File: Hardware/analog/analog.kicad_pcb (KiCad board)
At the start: 4 copper layers, 128 x 182 mm, 131 parts, among them J201 Würth 74651194R, J202 Würth 74651194R, J301 Conn_02x10_Odd_Even, J501 Conn_01x01, J502 Conn_01x01, M501 Fan_4pin, Q201 IXTH80N075L2, Q202 IXTH80N075L2, Q501 MMBT3904, U201 ADA4522-2, U202 LM431SC, U203 LMT86LMT, U204 ADA4522-2, U205 LM431SC, U206 LMT86LMT, U301 ADUM131D, U302 ADUM131D, U303 ADUM1250, U304 74LVC1G19, U305 AT24CS32-SSHM, U401 ICL7660, U402 MCP1804x-C002xMB, U403 MCP1703AT-5002E/DB, U404 XC6203E33, U405 LP5907MFX-3.3, U501 EMC2101-R, U601 MCP3562, U602 MAX6166, U603 DAC8562, U701 Si5351A-B-GT, Y701 25MHz

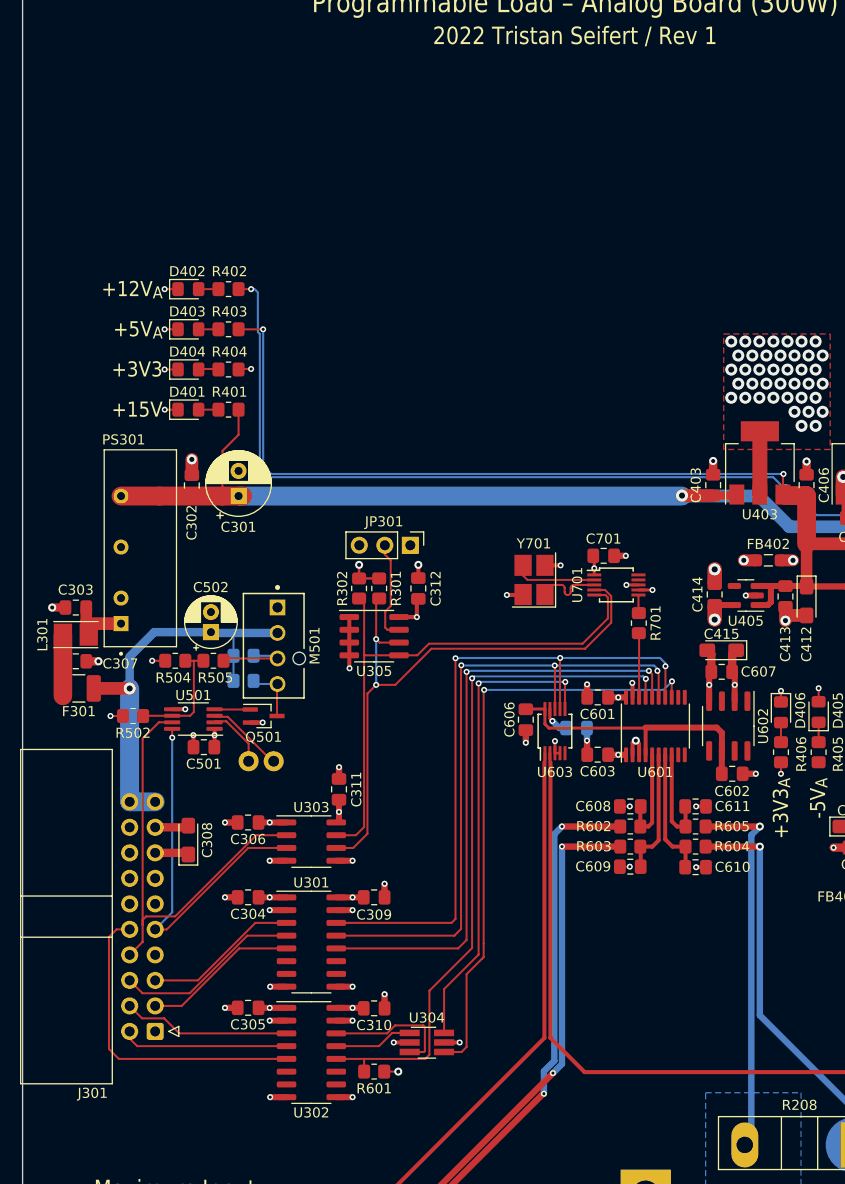
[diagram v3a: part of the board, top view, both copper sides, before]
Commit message: Moved analog board connector
- It now lines up properly with the one on the controller after it's
  been moved; there's still a bunch of un-done (power supply) stuff that
  needs to be re-routed or laid out better
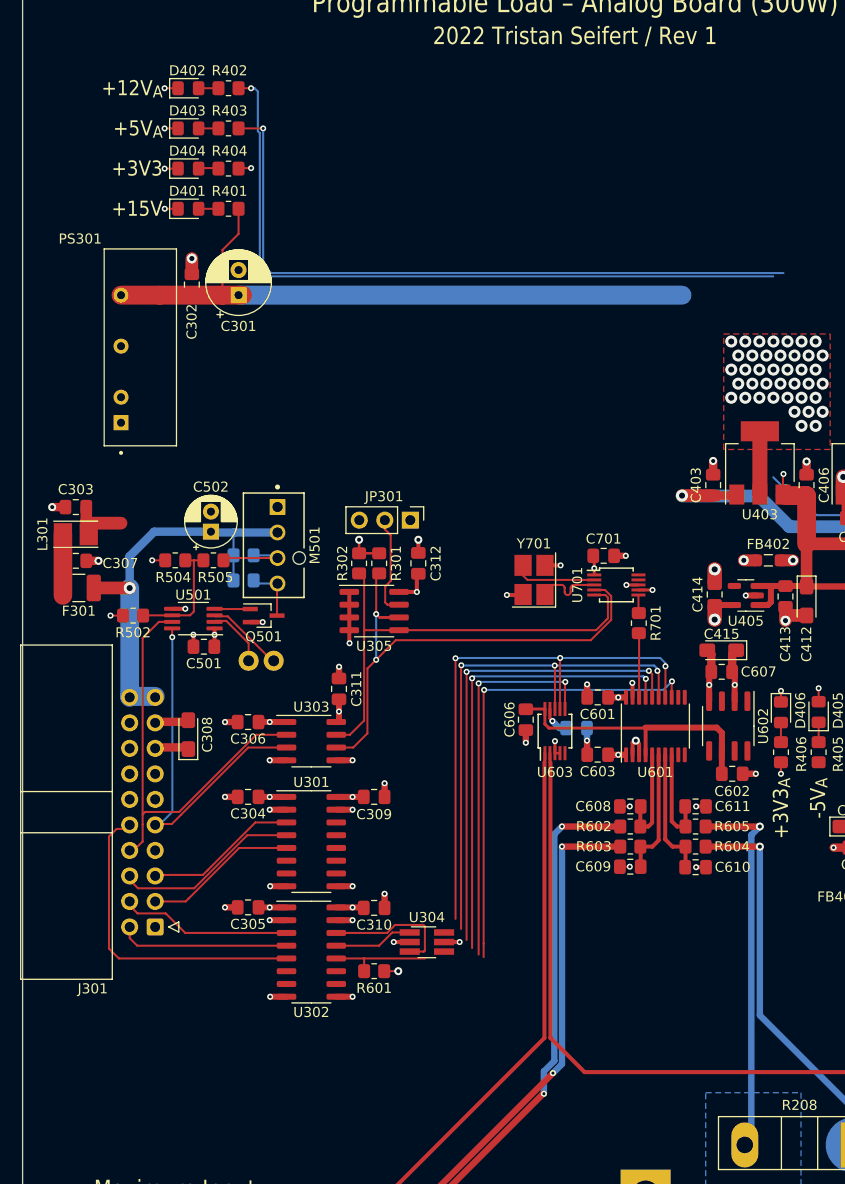
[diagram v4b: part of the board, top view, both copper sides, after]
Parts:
- moved C302 20.0 mm to (36.9, 53.0)
- moved D401 20.0 mm to (36.5, 45.5)
- moved D402 20.0 mm to (36.5, 33.5)
- moved D403 20.0 mm to (36.5, 37.5)
- moved D404 20.0 mm to (36.5, 41.5)
- moved PS301 20.0 mm to (29.8, 66.8)
- moved R401 20.0 mm to (40.5, 45.5)
- moved R402 20.0 mm to (40.5, 33.5)
- moved R403 20.0 mm to (40.5, 37.5)
- moved R404 20.0 mm to (40.5, 41.5)
- moved C301 20.0 mm to (41.5, 54.1)
- moved C308 10.5 mm to (36.5, 97.8)
- moved J301 10.4 mm to (33.2, 117.0)
- moved C303 10.0 mm to (25.3, 75.2)
- moved C304 10.0 mm to (42.5, 104.0)
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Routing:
- net /Analog stuff/SPI_MISO: track 61.0 -> 47.7 mm
- net /Analog stuff/~{IRQ}: track 69.3 -> 56.3 mm
- net /Analog stuff/SPI_MOSI: track 65.9 -> 53.2 mm
- net /Analog stuff/~{CS_ADC}: track 59.4 -> 47.3 mm
- net /Analog stuff/SPI_SCK: track 67.6 -> 55.6 mm
- net /Analog stuff/~{CS_DAC}: track 47.6 -> 38.4 mm
- net /I2C_SDA: track 55.2 -> 46.3 mm
- net /I2C_SCL: track 60.1 -> 53.8 mm
- net IN_I2C_SDA: track 44.0 -> 43.3 mm
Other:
- board text removed: "TODO: move connector"

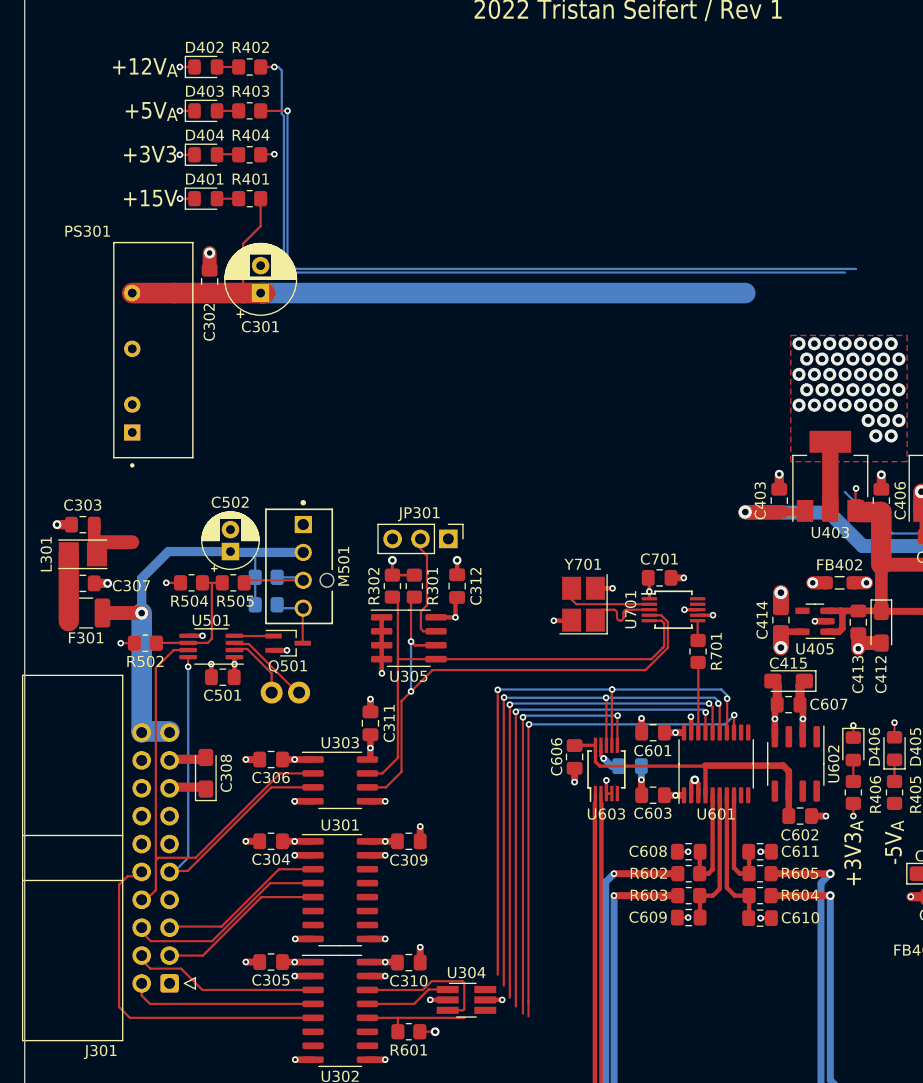
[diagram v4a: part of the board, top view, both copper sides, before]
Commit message: Analog board tweaks
- Moved a few traces and components around to accomodate other changes
  in the controller stuff, preparation for some sort of cleanup

- Aesthetic moves of labels on controller board
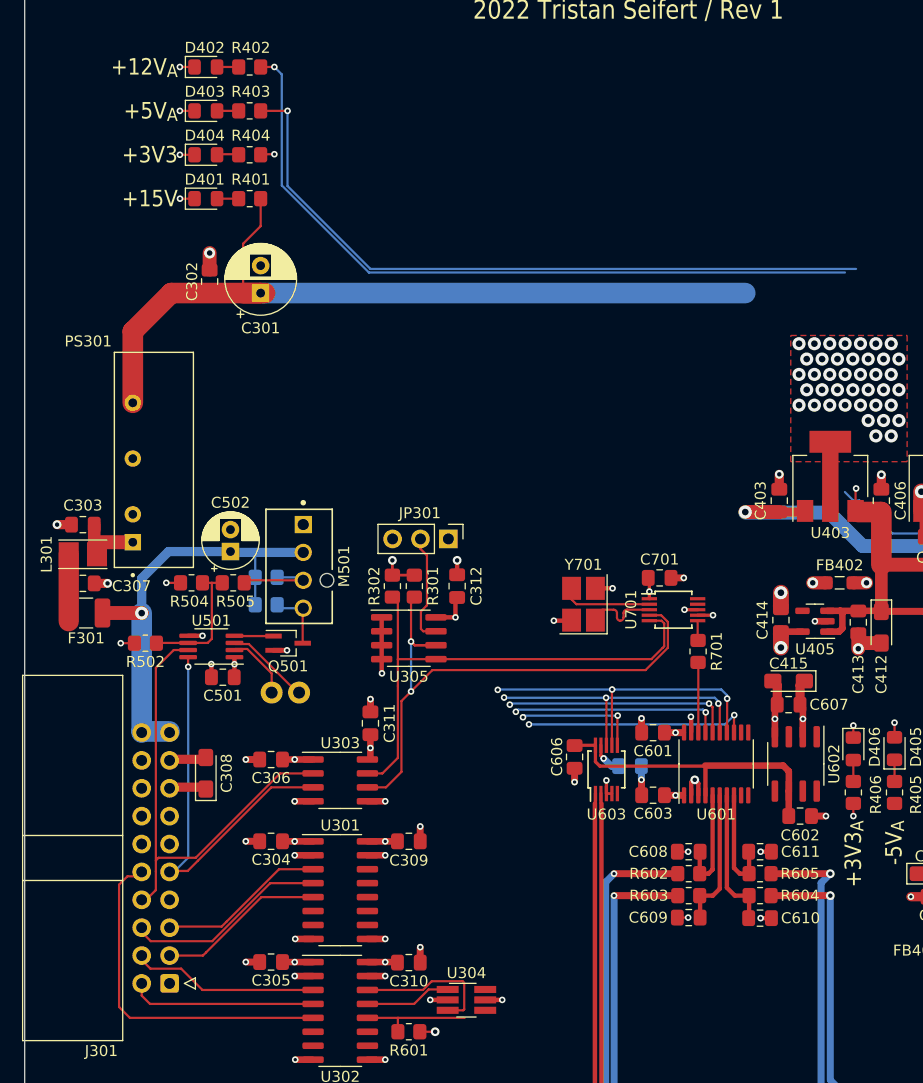
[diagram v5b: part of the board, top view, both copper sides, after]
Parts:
- R502: value 10k -> 5k6
- moved PS301 10.0 mm to (29.9, 76.8)
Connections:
- net /ISet_{0 renamed /ISet_{0}
- net /ISet_{1 renamed /ISet_{1}
- Q201 pad 3: /ISense_{0 -> /MOSFET Load/ISense_{0}
- Q202 pad 3: /ISense_{1 -> /MOSFET Load/ISense_{1}
- R201 pad 1: /ISense_{0 -> /MOSFET Load/ISense_{0}
- R204 pad 2: /ISense_{0 -> /MOSFET Load/ISense_{0}
- R208 pad 1: /ISense_{1 -> /MOSFET Load/ISense_{1}
- R211 pad 2: /ISense_{1 -> /MOSFET Load/ISense_{1}
- R602 pad 1: /ISense_{0 -> /ISense_{0}
- R604 pad 1: /ISense_{1 -> /ISense_{1}
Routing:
- net /MOSFET Load/ISense_{0}: track 0.00 -> 169.8 mm, vias 0 -> 3
- net /ISense_{0: track 169.8 -> 0.00 mm, vias 3 -> 0
- net /MOSFET Load/ISense_{1}: track 0.00 -> 55.8 mm, vias 0 -> 1
- net /ISense_{1: track 55.8 -> 0.00 mm, vias 1 -> 0
- net /Analog stuff/~{CS_DAC}: track 38.4 -> 11.4 mm
- net /Analog stuff/~{IRQ}: track 56.3 -> 29.5 mm
- net /Analog stuff/SPI_MISO: track 47.7 -> 21.0 mm
- net /Analog stuff/~{CS_ADC}: track 47.3 -> 20.7 mm
- net /Analog stuff/SPI_MOSI: track 53.2 -> 26.9 mm
- net /Analog stuff/SPI_SCK: track 55.6 -> 29.6 mm
- net +15V: track 96.6 -> 106.1 mm
- net +12VA: track 260.0 -> 255.9 mm
- net +5VA: track 147.3 -> 143.3 mm
